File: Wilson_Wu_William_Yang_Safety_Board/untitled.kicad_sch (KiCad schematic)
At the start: 10 parts, among them J11 XT60-M, J3 430450200, J5 430450200, U16 J115F11AH12VDCS61.5U

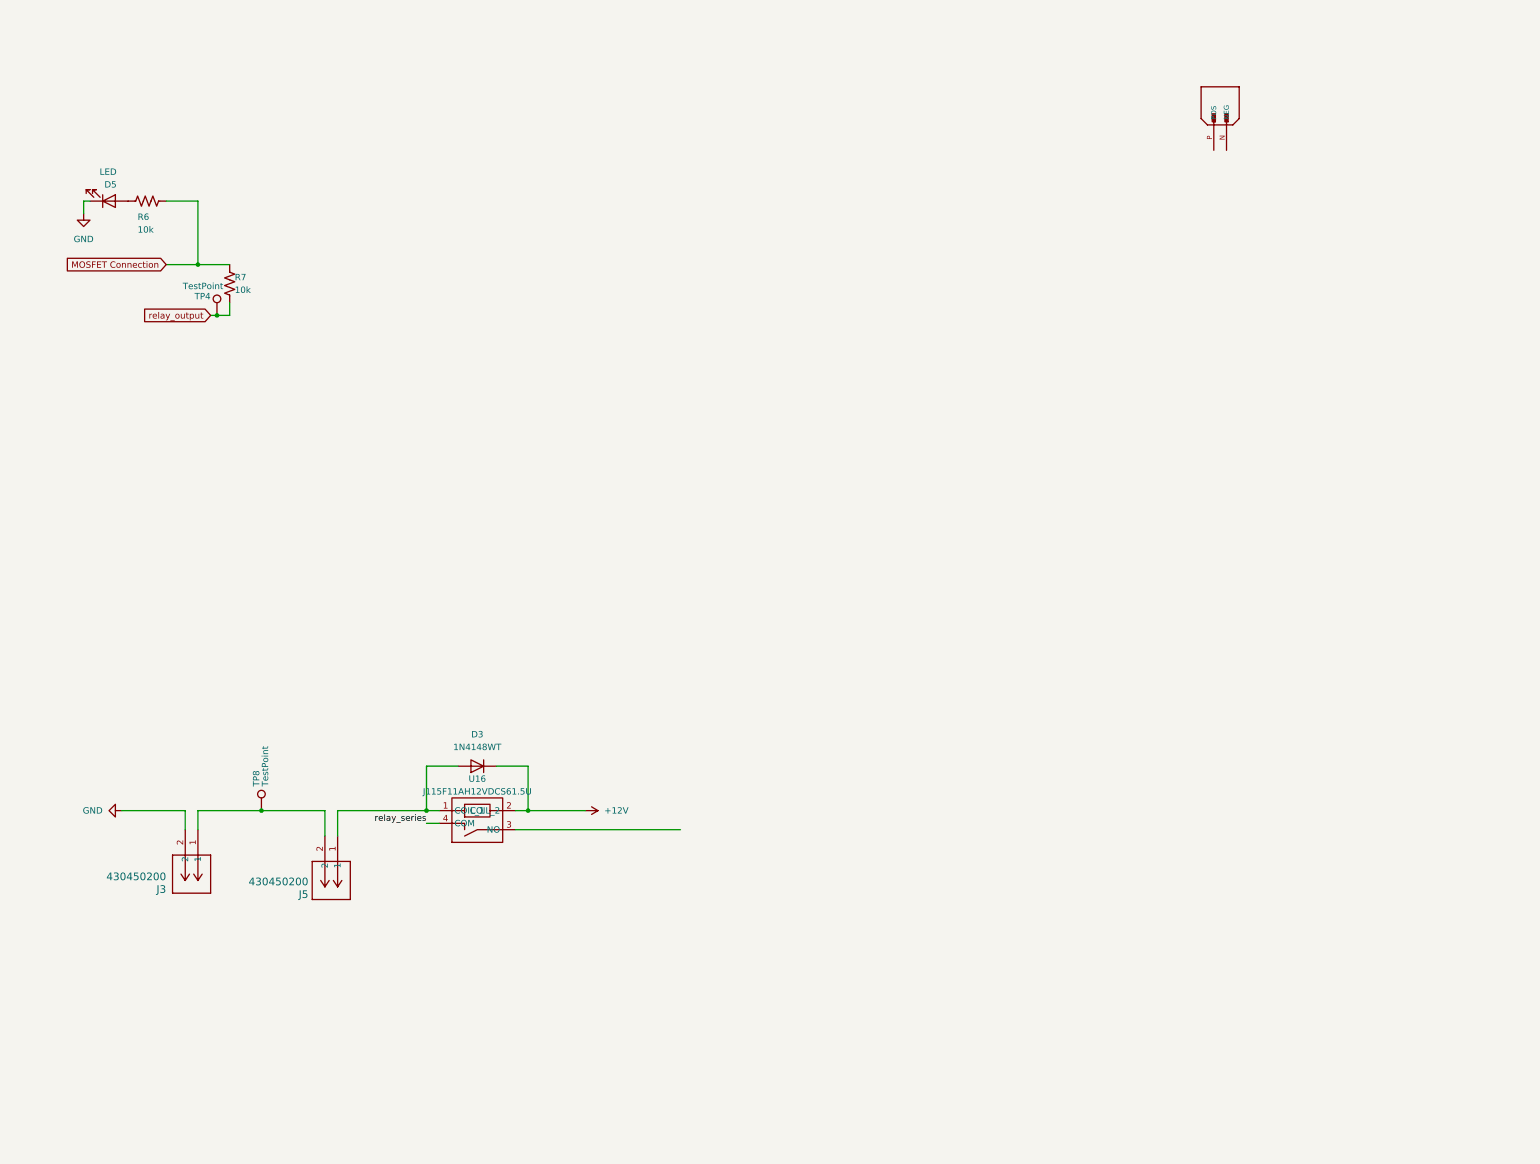
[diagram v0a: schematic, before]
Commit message: added relays
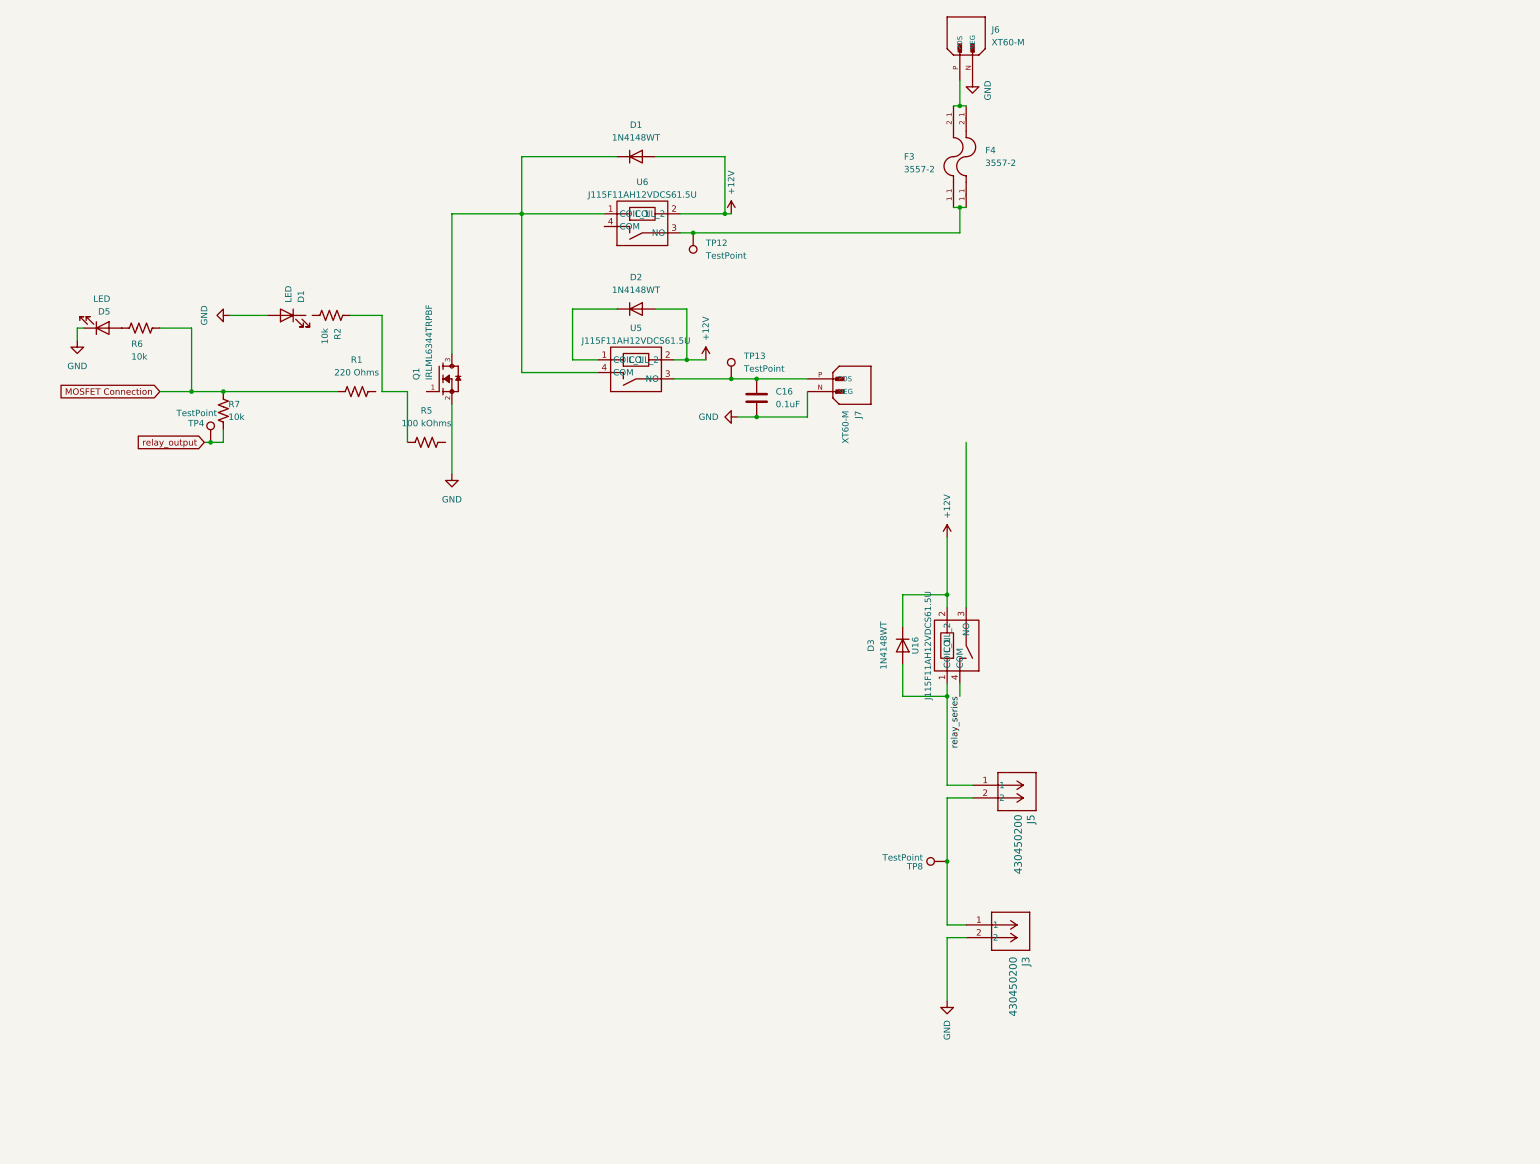
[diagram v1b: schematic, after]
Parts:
- removed J11: XT60-M, SMV_Connectors:AMASS_XT60-M, symbol SMV_Custom:XT60-M
- added C16: 0.1uF, Capacitor_SMD:C_0805_2012Metric, symbol Device:C
- added D1, D2: 1N4148WT, Diode_SMD:D_SOD-523, symbol Diode:1N4148WT
- added D1: LED, LED_SMD:LED_Foshan-NTD3528_3.5x2.8mm, symbol Device:LED
- added F3, F4: 3557-2, SMV_Connectors:FUSE_3557-2, symbol SMV_Custom:3555-2
- added J6, J7: XT60-M, SMV_Connectors:AMASS_XT60-M, symbol SMV_Custom:XT60-M
- added Q1: IRLML6344TRPBF, Test:TRANS_IRLML6344TRPBF, symbol IRLML6344TRPBF:IRLML6344TRPBF
- added R1: 220 Ohms, Resistor_SMD:R_0805_2012Metric, symbol Device:R_US
- added R2: 10k, Resistor_SMD:R_0805_2012Metric, symbol Device:R_US
- added R5: 100 kOhms, Resistor_SMD:R_0805_2012Metric, symbol Device:R_US
- added TP12, TP13: TestPoint, TestPoint:TestPoint_Loop_D2.54mm_Drill1.5mm_Beaded, symbol Connector:TestPoint
- added U5, U6: J115F11AH12VDCS61.5U, SMV_Passives:J115F11AH12VDCS615U, symbol SMV_Custom:J115F11AH12VDCS61.5U
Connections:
- net +12V: now also D1.2 (A), D2.2 (A), U5.2 (COIL_2), U6.2 (COIL_2)
- net GND: now also C16.1, D1.2 (A), J6.N (NEG), J7.N (NEG), Q1.2
- net MOSFET Connection: now also R1.2
- new net: C16.2, J7.P (POS), TP13.1, U5.3 (NO)
- new net: R2.2, R5.1
- new net: F3.1_1, F4.1_1, TP12.1, U6.3 (NO)
- new net: F3.2_1, F4.2_1, J6.P (POS)
- new net: D1.1 (K), Q1.3, U5.4 (COM), U6.1 (COIL_1)
- new net: D2.1 (K), U5.1 (COIL_1)
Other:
- moved on the sheet: D3, D5, J3, J5, R6, R7, TP4, TP8, U16

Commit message: sch
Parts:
- added C13: 1nF, SMV_Passives:CAPC17595_87N_KEM, symbol Device:C
- added C15: 100nF, SMV_Passives:CAPC17595_87N_KEM, symbol Device:C
- added C17: 3.3nF, SMV_Passives:CAPC17595_87N_KEM, symbol Device:C
- added C19: 100uF, SMV_Passives:CAPC17595_87N_KEM, symbol Device:C_US
- added D4: 68V, symbol Device:D_Zener
- added F1, F2: 3557-2, SMV_Connectors:FUSE_3557-2, symbol SMV_Custom:3555-2
- added Q2: IRLML6344TRPBF, Test:TRANS_IRLML6344TRPBF, symbol IRLML6344TRPBF:IRLML6344TRPBF
- added Q3, Q4: NTBLS0D8N08XTXG, H-PSOF8L_100CU_ONS_OSI, symbol SMV_beefy_FET:NTBLS0D8N08XTXG
- added R10, R4, R9: 10k, SMV_Passives:0603_resistors, symbol Device:R_US
- added R10: 100k, SMV_Passives:0603_resistors, symbol Device:R_US
- added R15: 0.1, SMV_Passives:0603_resistors, symbol Device:R_US
- added R3: 2.2k, SMV_Passives:0603_resistors, symbol Device:R_US
- added R3: 191k, SMV_Passives:0603_resistors, symbol Device:R_US
- added R4: R_US, SMV_Passives:0603_resistors, symbol Device:R_US
- added R8: 1.2m, SMV_Passives:0603_resistors, symbol Device:R_US
- added R8: 470k, SMV_Passives:0603_resistors, symbol Device:R_US
- added R9: 432k, SMV_Passives:0603_resistors, symbol Device:R_US
- added U10: LTC4364HS, Package_SO:SOIC-16_3.9x9.9mm_P1.27mm, symbol Power_Management:LTC4364HS
- C16: value 0.1uF -> 6.8nF; footprint Capacitor_SMD:C_0805_2012Metric -> SMV_Passives:CAPC17595_87N_KEM
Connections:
- net GND: now also C13.2, C15.2, C17.2, D4.2 (A), Q2.2, R10.2, R15.2, R4.2, R9.2, U10.12 (GND); no longer J3.2, J6.N (NEG), J7.N (NEG)
- net at J7.P (POS), TP13.1: now also F1.2_1, F2.2_1; no longer C16.2, U5.3 (NO)
- net at R2.1: now also D1.1 (K)
- net at R2.2, R5.1: now also R1.1
- net relay conn: now reaches U16.3 (NO)
- net relay conn: now also Q3.9, R10.1, R3.1, R3.1, R8.1
- net estop conn: now reaches TP12.1, U6.3 (NO)
- net estop conn: now also J3.2; no longer F3.1_1, F4.1_1
- net at D1.1 (K), Q1.3, U6.1 (COIL_1): no longer U5.4 (COM)
- net at Q1.1: now also R5.2, Q2.1
- net at D2.1 (K), U5.1 (COIL_1): now also Q2.3
- net at U6.4 (COM): now also F1.1_1, F2.1_1
- new net: J7.N (NEG), U5.4 (COM)
- new net: C16.2, Q3.2, Q3.3, Q3.4, Q4.1, Q4.2, Q4.3, Q4.4, R4.1, U10.4 (DGATE), U10.5 (SOURCE), U10.6 (HGATE)
- new net: C19.2, R15.1
- new net: R10.1, R9.2, U10.16 (FB)
- new net: Q4.9, R8.1, U10.2 (SENSE)
- new net: C17.1, U10.15 (TMR)
- new net: J6.N (NEG), U5.3 (NO)
- new net: C13.1, R8.2, R9.1, U10.11 (OV)
- new net: C15.1, R3.2, R4.1, U10.10 (UV)
- new net: D4.1 (K), R3.2, U10.8 (VCC)
- new net: R10.2, U10.9 (~{SHDN})
- new net: Q4.5, Q4.6, Q4.7, Q4.8
- new net: Q3.1, R4.2
- new net: Q3.5, Q3.6, Q3.7, Q3.8
- new net source conn: C19.1, F3.1_1, F4.1_1, R8.2, R9.1, U10.1 (OUT)
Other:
- note added: "30-50V"
- note added: "At least 22uF"
- note added: "Cgate"
- note added: "Ctmr"
- moved on the sheet: D2, D3, J3, J5, J6, J7, R5, TP13, TP8, U16, U5

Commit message: sch change
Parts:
- removed D1: LED, LED_SMD:LED_Foshan-NTD3528_3.5x2.8mm, symbol Device:LED
- removed R2: 10k, Resistor_SMD:R_0805_2012Metric, symbol Device:R_US
- removed R5: 100 kOhms, Resistor_SMD:R_0805_2012Metric, symbol Device:R_US
- R1: value 220 Ohms -> 330 ohms
- renumbered C13 to C101, C15 to C102, C16 to C103, C19 to C104, R8 to R101, R3 to R102, R10 to R103, R3 to R104, R4 to R105, R8 to R106, R9 to R107, R10 to R108, R15 to R109
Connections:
- net relay_series is gone; now on net estop conn: U16.4 (COM)
- net GND: now also J3.2
- net estop conn: no longer J3.2
- net relay conn: no longer U16.3 (NO)
- net source conn: now also U16.3 (NO)
- net at R1.1: now also Q1.1, Q2.1

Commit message: sch changes
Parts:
- removed C101: 1nF, SMV_Passives:CAPC17595_87N_KEM, symbol Device:C
- removed C102: 100nF, SMV_Passives:CAPC17595_87N_KEM, symbol Device:C
- removed C103: 6.8nF, SMV_Passives:CAPC17595_87N_KEM, symbol Device:C
- removed C104: 100uF, SMV_Passives:CAPC17595_87N_KEM, symbol Device:C_US
- removed C17: 3.3nF, SMV_Passives:CAPC17595_87N_KEM, symbol Device:C
- removed D4: 68V, symbol Device:D_Zener
- removed F1, F2: 3557-2, SMV_Connectors:FUSE_3557-2, symbol SMV_Custom:3555-2
- removed Q3, Q4: NTBLS0D8N08XTXG, H-PSOF8L_100CU_ONS_OSI, symbol SMV_beefy_FET:NTBLS0D8N08XTXG
- removed R101: 470k, SMV_Passives:0603_resistors, symbol Device:R_US
- removed R102: 191k, SMV_Passives:0603_resistors, symbol Device:R_US
- removed R103: 100k, SMV_Passives:0603_resistors, symbol Device:R_US
- removed R104: 2.2k, SMV_Passives:0603_resistors, symbol Device:R_US
- removed R105: R_US, SMV_Passives:0603_resistors, symbol Device:R_US
- removed R106: 1.2m, SMV_Passives:0603_resistors, symbol Device:R_US
- removed R107: 432k, SMV_Passives:0603_resistors, symbol Device:R_US
- removed R108, R4, R9: 10k, SMV_Passives:0603_resistors, symbol Device:R_US
- removed R109: 0.1, SMV_Passives:0603_resistors, symbol Device:R_US
- removed U10: LTC4364HS, Package_SO:SOIC-16_3.9x9.9mm_P1.27mm, symbol Power_Management:LTC4364HS
- added D6: LED, LED_SMD:LED_Foshan-NTD3528_3.5x2.8mm, symbol Device:LED
- added R2: 10k, Resistor_SMD:R_0805_2012Metric, symbol Device:R_US
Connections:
- net +12V: now also D1.1 (K), D2.1 (K), U5.1 (COIL_1), R2.2; no longer D1.2 (A), D2.2 (A), U5.2 (COIL_2)
- net GND: now also D6.1 (K)
- net estop conn: now also U16.3 (NO), U6.4 (COM); no longer TP12.1, U16.4 (COM), U6.3 (NO)
- net load negative: now reaches J7.N (NEG), U5.4 (COM)
- net load conn: now reaches J7.P (POS), TP13.1
- net at Q1.3, U6.1 (COIL_1): now also D1.2 (A); no longer D1.1 (K)
- net at D3.2 (A), U16.1 (COIL_1): no longer J5.1
- net source negative: now reaches J6.N (NEG), U5.3 (NO)
- net source conn renamed source_conn
- net source_conn: now also J5.1, U16.4 (COM); no longer U16.3 (NO)
- new net: D6.2 (A), R2.1
- new net: D2.2 (A), Q2.3, U5.2 (COIL_2)
- new net load switch conn: TP12.1, U6.3 (NO)
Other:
- added sheet Load Switch (load_switch.kicad_sch)
- note added: "Load"
- note added: "Source"
- note removed: "30-50V"
- note removed: "At least 22uF"
- note removed: "Cgate"
- note removed: "Ctmr"
- moved on the sheet: D1, D2, D3, D5, F3, F4, J3, J5, J6, J7, Q1, Q2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
